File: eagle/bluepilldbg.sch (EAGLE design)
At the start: 9 parts

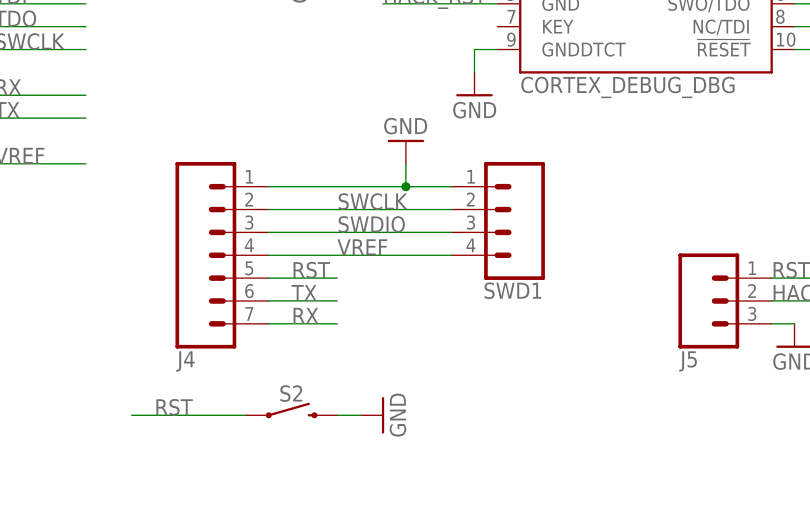
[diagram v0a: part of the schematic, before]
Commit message: smaller pcb
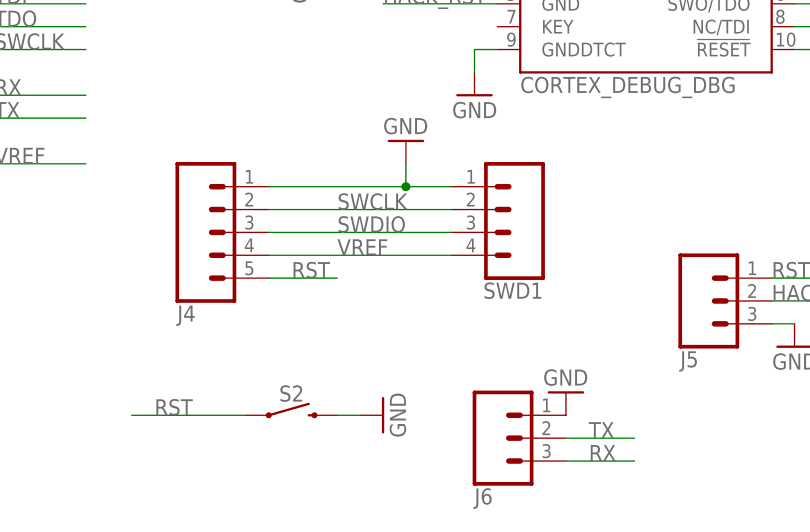
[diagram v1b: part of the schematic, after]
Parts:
- added J6: (no value), pcnt:CONN_031X03_NO_SILK
- J4: device SparkFun-Connectors:CONN_07NO_SILK -> pcnt:CONN_05SMALLHOLE
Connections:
- net GND: now also J6.1
- net RX: now also J6.3; no longer J4.7
- net TX: now also J6.2; no longer J4.6
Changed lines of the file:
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@@
 <part name="P+2" library="mb-arcade-shield" deviceset="VCC" device=""/>
 <part name="GND6" library="BrainPad MAX" deviceset="GND" device=""/>
-<part name="J4" library="SparkFun-Connectors" deviceset="CONN_07" device="NO_SILK"/>
 <part name="J5" library="pcnt" deviceset="CONN_03" device="1X03_NO_SILK"/>
 <part name="GND5" library="BrainPad MAX" deviceset="GND" device=""/>
+<part name="J6" library="pcnt" deviceset="CONN_03" device="1X03_NO_SILK"/>
+<part name="GND7" library="BrainPad MAX" deviceset="GND" device=""/>
+<part name="J4" library="pcnt" deviceset="CONN_05" device="SMALLHOLE"/>
 </parts>
 <sheets>
@@
 <attribute name="VALUE" x="10.16" y="48.26" size="1.778" layer="96" rot="MR270"/>
 </instance>
-<instance part="J4" gate="J1" x="-10.16" y="66.04" smashed="yes" rot="MR180">
-<attribute name="VALUE" x="-15.24" y="75.946" size="1.778" layer="96" font="vector" rot="MR180"/>
-<attribute name="NAME" x="-15.24" y="52.832" size="1.778" layer="95" font="vector" rot="MR180"/>
-</instance>
 <instance part="J5" gate="J$1" x="43.18" y="58.42" smashed="yes" rot="MR180">
 <attribute name="VALUE" x="40.64" y="65.786" size="1.778" layer="96" font="vector" rot="MR180"/>
@@
 <instance part="GND5" gate="1" x="53.34" y="53.34" smashed="yes" rot="MR0">
 <attribute name="VALUE" x="55.88" y="50.8" size="1.778" layer="96" rot="MR0"/>
+</instance>
+<instance part="J6" gate="J$1" x="20.32" y="43.18" smashed="yes" rot="MR180">
+<attribute name="VALUE" x="17.78" y="50.546" size="1.778" layer="96" font="vector" rot="MR180"/>
+<attribute name="NAME" x="17.78" y="37.592" size="1.778" layer="95" font="vector" rot="MR180"/>
+</instance>
+<instance part="GND7" gate="1" x="27.94" y="48.26" smashed="yes" rot="MR180">
+<attribute name="VALUE" x="25.4" y="50.8" size="1.778" layer="96" rot="MR180"/>
+</instance>
+<instance part="J4" gate="G$1" x="-12.7" y="66.04" smashed="yes" rot="MR180">
+<attribute name="VALUE" x="-15.24" y="75.946" size="1.778" layer="96" font="vector" rot="MR180"/>
+<attribute name="NAME" x="-15.24" y="57.912" size="1.778" layer="95" font="vector" rot="MR180"/>
 </instance>
 </instances>
@@
 <wire x1="10.16" y1="73.66" x2="10.16" y2="71.12" width="0.1524" layer="91"/>
 <junction x="10.16" y="71.12"/>
-<pinref part="J4" gate="J1" pin="1"/>
+<pinref part="J4" gate="G$1" pin="1"/>
 </segment>
 <segment>
@@
 <wire x1="53.34" y1="55.88" x2="50.8" y2="55.88" width="0.1524" layer="91"/>
 </segment>
+<segment>
+<pinref part="J6" gate="J$1" pin="1"/>
+<pinref part="GND7" gate="1" pin="GND"/>
+</segment>
 </net>
 <net name="RST" class="0">
@@
 <wire x1="-5.08" y1="60.96" x2="2.54" y2="60.96" width="0.1524" layer="91"/>
 <label x="-2.54" y="60.96" size="1.778" layer="95"/>
-<pinref part="J4" gate="J1" pin="5"/>
+<pinref part="J4" gate="G$1" pin="5"/>
 </segment>
 <segment>
@@
 <wire x1="15.24" y1="66.04" x2="-5.08" y2="66.04" width="0.1524" layer="91"/>
 <label x="2.54" y="66.04" size="1.778" layer="95"/>
-<pinref part="J4" gate="J1" pin="3"/>
+<pinref part="J4" gate="G$1" pin="3"/>
 </segment>
 </net>
@@
 <wire x1="15.24" y1="68.58" x2="-5.08" y2="68.58" width="0.1524" layer="91"/>
 <label x="2.54" y="68.58" size="1.778" layer="95"/>
-<pinref part="J4" gate="J1" pin="2"/>
+<pinref part="J4" gate="G$1" pin="2"/>
 </segment>
 </net>
@@
 </segment>
 <segment>
-<wire x1="-5.08" y1="55.88" x2="2.54" y2="55.88" width="0.1524" layer="91"/>
-<label x="-2.54" y="55.88" size="1.778" layer="95"/>
-<pinref part="J4" gate="J1" pin="7"/>
+<wire x1="27.94" y1="40.64" x2="35.56" y2="40.64" width="0.1524" layer="91"/>
+<label x="30.48" y="40.64" size="1.778" layer="95"/>
+<pinref part="J6" gate="J$1" pin="3"/>
 </segment>
 </net>
@@
 </segment>
 <segment>
-<wire x1="-5.08" y1="58.42" x2="2.54" y2="58.42" width="0.1524" layer="91"/>
-<label x="-2.54" y="58.42" size="1.778" layer="95"/>
-<pinref part="J4" gate="J1" pin="6"/>
+<wire x1="27.94" y1="43.18" x2="35.56" y2="43.18" width="0.1524" layer="91"/>
+<label x="30.48" y="43.18" size="1.778" layer="95"/>
+<pinref part="J6" gate="J$1" pin="2"/>
 </segment>
 </net>
@@
 <wire x1="15.24" y1="63.5" x2="-5.08" y2="63.5" width="0.1524" layer="91"/>
 <label x="2.54" y="63.5" size="1.778" layer="95"/>
-<pinref part="J4" gate="J1" pin="4"/>
-</segment>
-<segment>
+<pinref part="J4" gate="G$1" pin="4"/>
+</segment>
+<segment>

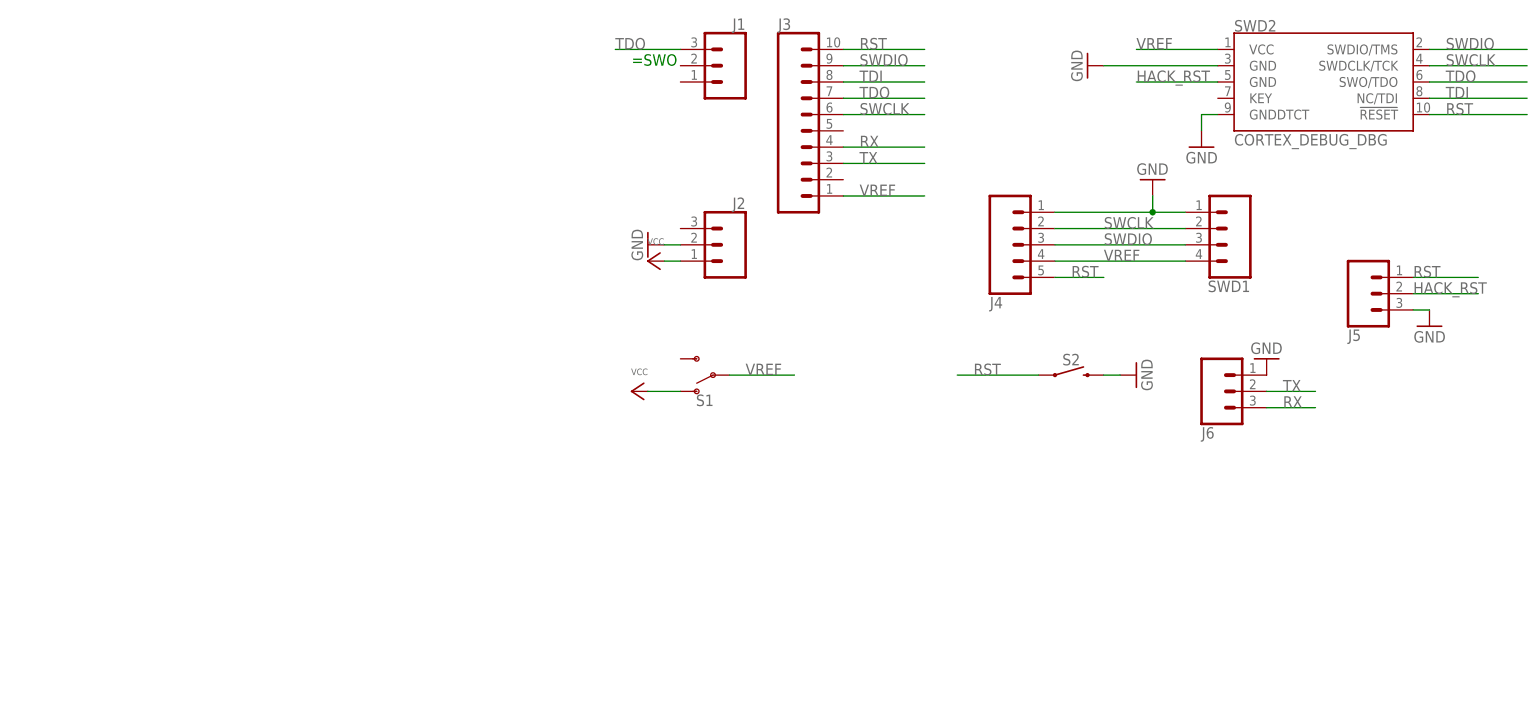
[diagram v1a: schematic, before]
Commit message: Nicer schematics; place part names
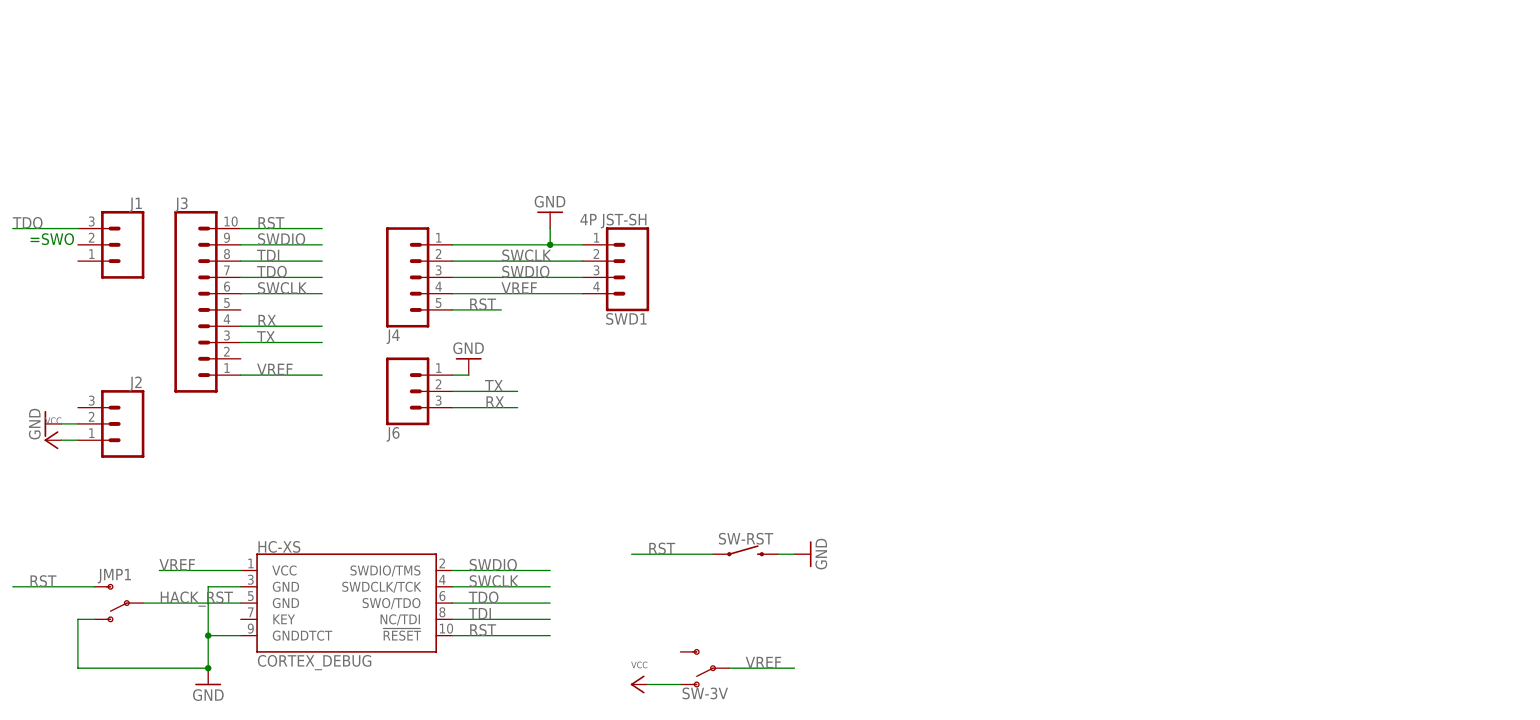
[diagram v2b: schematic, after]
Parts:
- removed J5: (no value), pcnt:CONN_031X03_NO_SILK
- removed S1: (no value), pcnt:SWITCH-SPDT-SMD-AYZ0202
- removed S2: MOMENTARY-SWITCH-SPST-SMD-6.0X3.5MM, mb-arcade-shield:MOMENTARY-SWITCH-SPST-SMD-6.0X3.5MM
- removed SWD2: CORTEX_DEBUG_DBG, pcnt:CORTEX_DEBUG_DBG
- added HC-XS: CORTEX_DEBUG, pcnt:CORTEX_DEBUG_DBG
- added JMP1: (no value), pcnt:SWITCH-SPDT-HD
- added SW-3V: (no value), pcnt:SWITCH-SPDT-SMD-AYZ0202
- added SW-RST: MOMENTARY-SWITCH-SPST-SMD-6.0X3.5MM, mb-arcade-shield:MOMENTARY-SWITCH-SPST-SMD-6.0X3.5MM
- SWD1: value (none) -> 4P JST-SH
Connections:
- net GND: now also HC-XS.GND@3, HC-XS.GNDDTCT, JMP1.O, SW-RST.2; no longer J5.3, S2.2, SWD2.GND@3, SWD2.GNDDTCT
- net HACK_RST: now also HC-XS.GND@5, JMP1.P; no longer J5.2, SWD2.GND@5
- net RST: now also HC-XS.!RESET, JMP1.S, SW-RST.1; no longer J5.1, S2.1, SWD2.!RESET
- net SWCLK: now also HC-XS.SWDCLK/TCK; no longer SWD2.SWDCLK/TCK
- net SWDIO: now also HC-XS.SWDIO/TMS; no longer SWD2.SWDIO/TMS
- net TDI: now also HC-XS.NC/TDI; no longer SWD2.NC/TDI
- net TDO: now also HC-XS.SWO/TDO; no longer SWD2.SWO/TDO
- net VCC: now also SW-3V.O; no longer S1.O
- net VREF: now also HC-XS.VCC, SW-3V.P; no longer S1.P, SWD2.VCC
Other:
- moved on the sheet: J1, J2, J3, J4, J6, SWD1

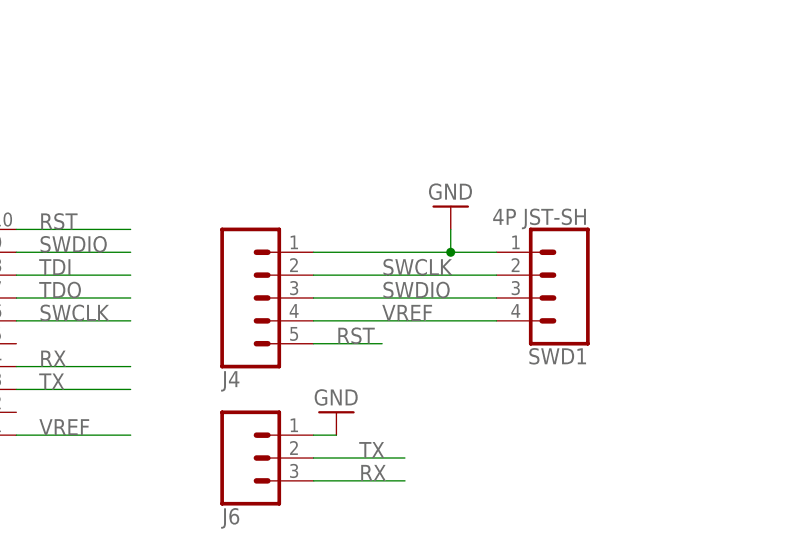
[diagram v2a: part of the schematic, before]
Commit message: Re-order JST-SH debug connector to match QWIIC
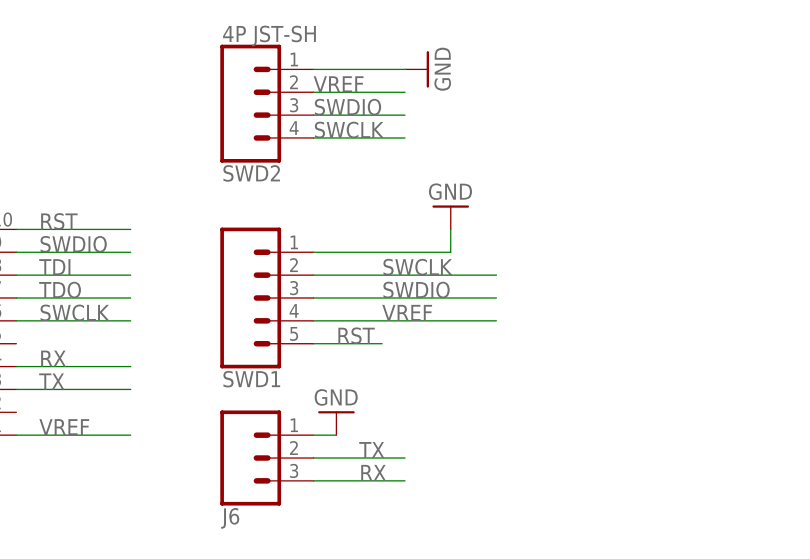
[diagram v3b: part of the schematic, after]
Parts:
- removed J4: (no value), pcnt:CONN_05SMALLHOLE
- added SWD2: 4P JST-SH, pcnt:CONN_04SMD2
- SWD1: value 4P JST-SH -> (none); device pcnt:CONN_04SMD2 -> pcnt:CONN_05SMALLHOLE
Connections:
- net GND: now also SWD2.1; no longer J4.1
- net RST: now also SWD1.5; no longer J4.5
- net SWCLK: now also SWD2.4; no longer J4.2
- net SWDIO: now also SWD2.3; no longer J4.3
- net VREF: now also SWD2.2; no longer J4.4
